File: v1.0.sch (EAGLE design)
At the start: 271 parts, among them J1 DC-044-A, J10 16p-2.54, J11 16p-2.54, J2 MICROSD-9P, J3 2p-2.54, J4 2p-2.54, J5 16p-2.54, J6 16p-2.54, J7 16p-2.54, J8 2p-2.54, J9 16p-2.54, Q1 32.768khZ@6Pf, Q2 SSM3J328R,LF, Q4 BSS138W-7-F, Q5 SSM3J328R,LF, SW1 TS-1101F, SW2 TS-1101F, SW3 TS-1101F, SW5 TS-1101F, U1 MCP23017-E/SO, U10 74HCT139D, U11 BZX84C30, U12 SP483ECN-L, U13 FT232RL-SSOP28, U14 FT232RL-SSOP28, U15 FT232RL-SSOP28, U2 MCP79412-I/SN, U3 LOPY, U4 MAX213IDBR, U5 FT232RL-SSOP28, U6 FT232RL-SSOP28, U8 BR24G32-3, Y2 12MHZ

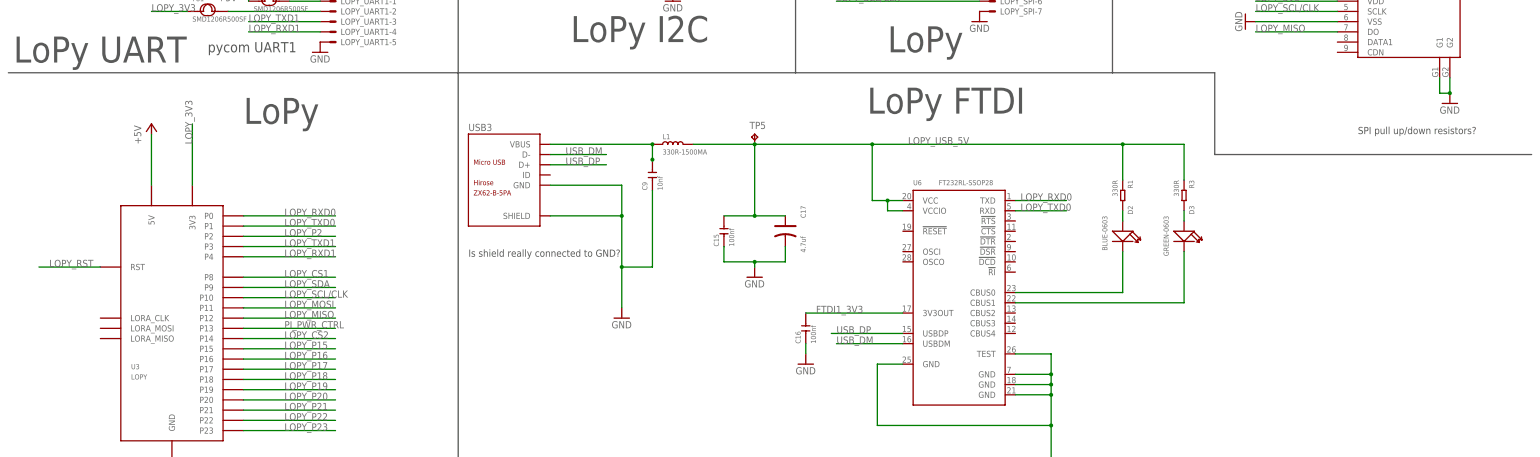
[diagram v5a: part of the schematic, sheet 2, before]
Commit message: Pi control of LoPy reset added Pi &  lopy uart0 connected
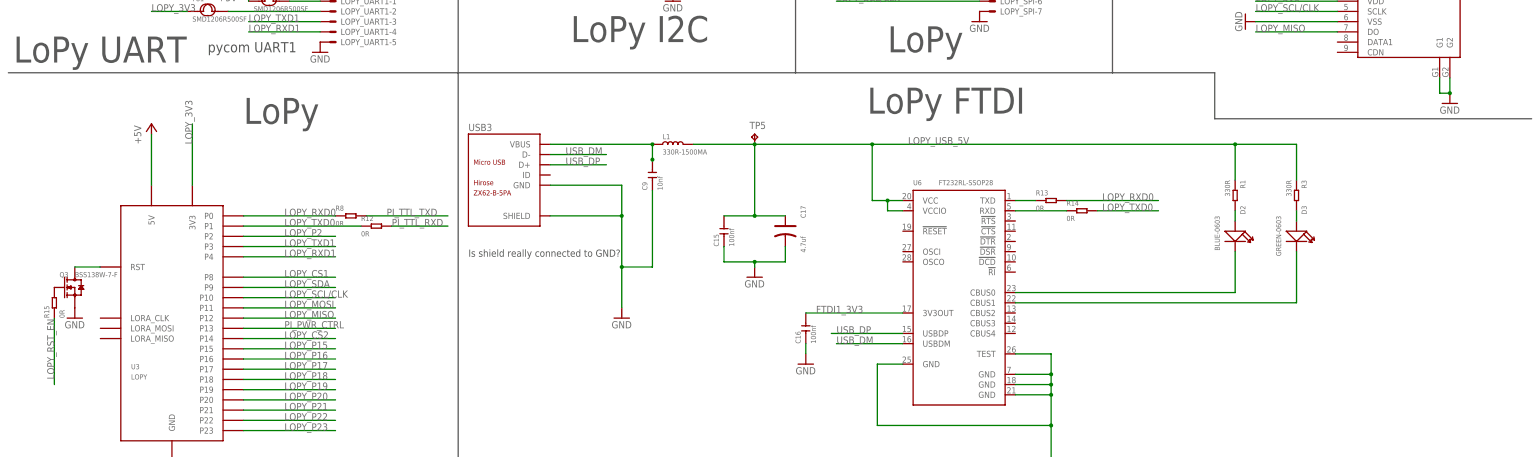
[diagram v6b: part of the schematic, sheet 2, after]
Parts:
- added Q3: BSS138W-7-F, Seeed-Transistor:SMD-MOSFET-N-CH-50V-200MA-BSS138W-7-F(SOT-23)
- added R12, R13, R14, R15, R8: 0R, Seeed-Resistor:SMD-RES-0R-5%-1/10W(0603)
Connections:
- removed net GPIO26_FREE: J10.14, J11.14, PCB1.GPIO26
- new net LOPY_RST_EN: PCB1.GPIO26, R15.1
- new net N$10: R14.1, U6.RXD
- new net N$12: Q3.G, R15.2
- new net N$8: R13.1, U6.TXD
- net GND: now also J10.14, J11.14, Q3.S
- net LOPY_RST: now also Q3.D
- net LOPY_RXD0: now also R13.2, R8.1; no longer U6.TXD
- net LOPY_TXD0: now also R12.1, R14.2; no longer U6.RXD
- net PI_TTL_RXD: now also R12.2
- net PI_TTL_TXD: now also R8.2
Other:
- note removed: "SPI pull up/down resistors?"
- moved on the sheet: D2, D3, R1, R3

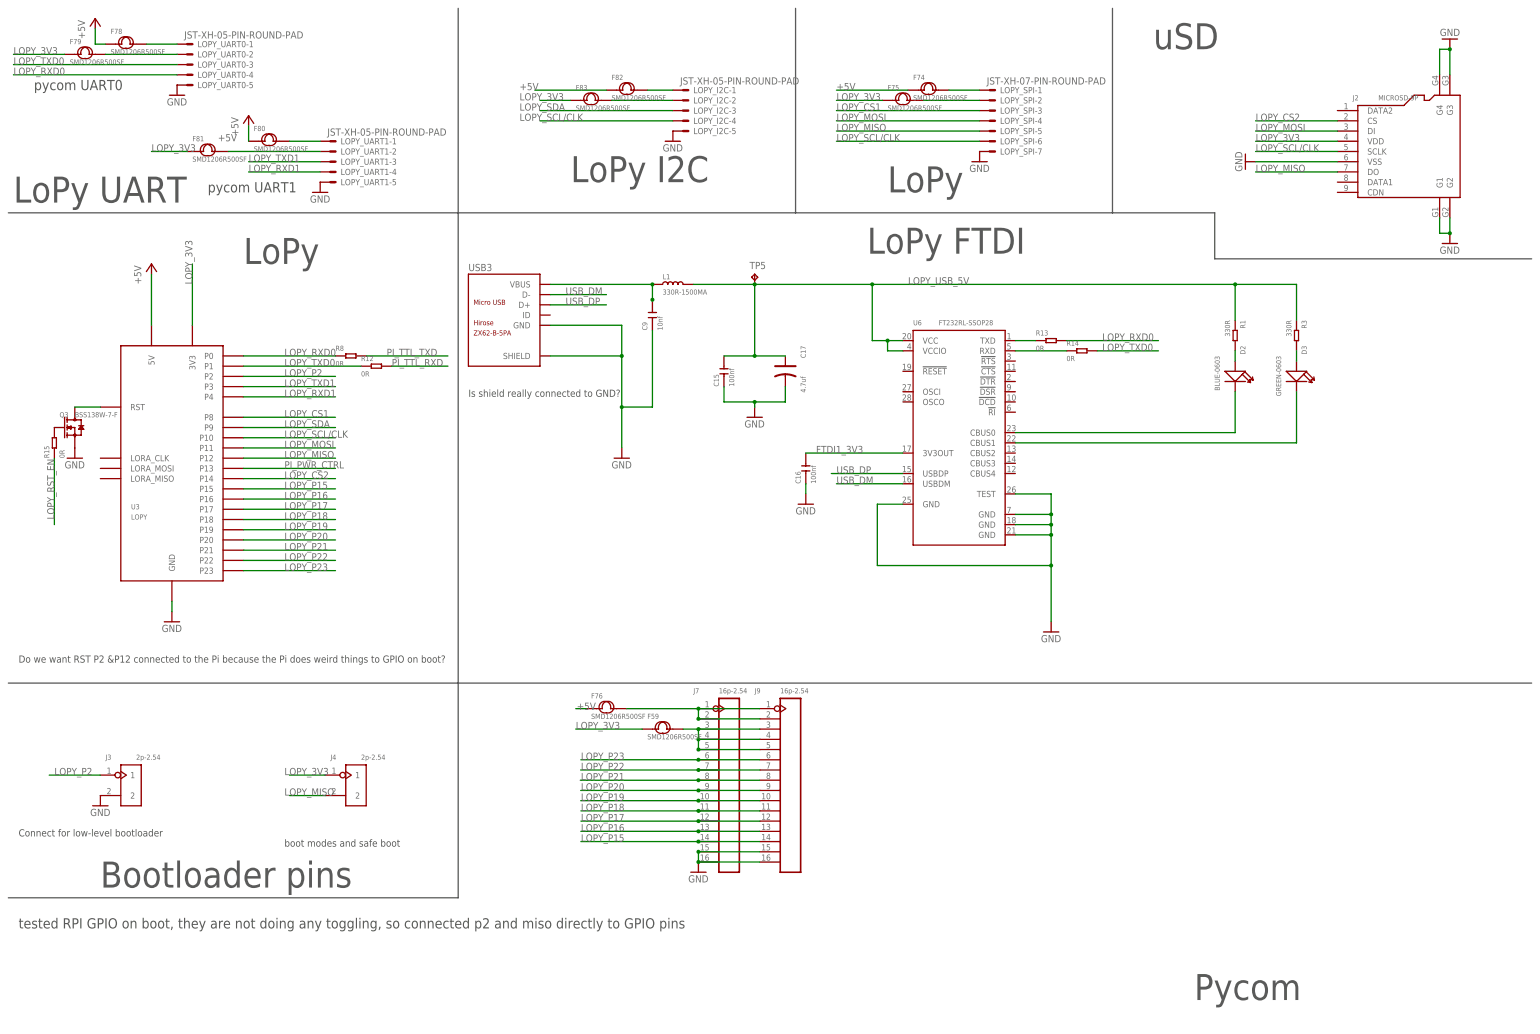
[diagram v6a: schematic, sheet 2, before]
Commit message: Switches changed for toggle as opposed to push FETs added for Pi -> lopy control lines
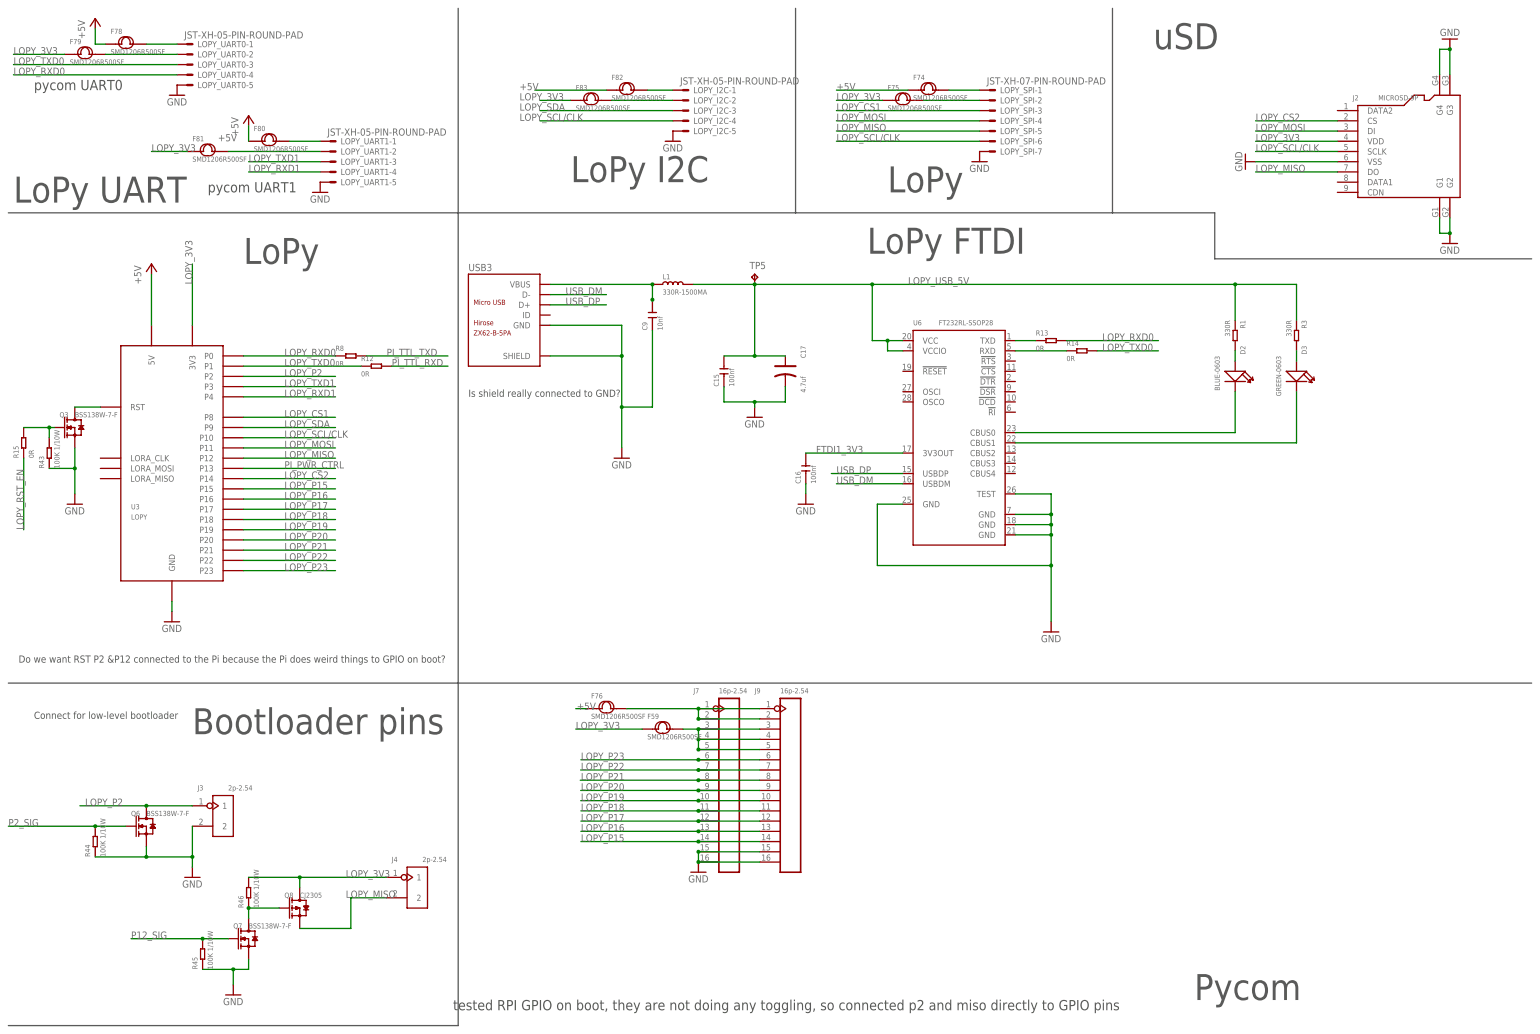
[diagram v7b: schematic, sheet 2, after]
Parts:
- removed R26: 22R, Seeed-Resistor-2016:SMD-RES-22R-5%-1/10W(0603)
- removed SW2: TS-1101F, Seeed-Switch:DIP-BUTTON(2P-6.0X3.0X4.3MM)-TS-1101F
- added Q6, Q7: BSS138W-7-F, Seeed-Transistor:SMD-MOSFET-N-CH-50V-200MA-BSS138W-7-F(SOT-23)
- added Q8: CJ2305, Seeed-Transistor:SMD-MOSFET-P-CH-8V-4.1A-CJ2305(SOT-23)
- added R43, R44, R45, R46: 100K 1/10W, Seeed-Resistor:SMD-RES-100K-5%-1/10W(0603)
- added SW4: MK-12C02 G1.5, Seeed-Switch:SMD-TOGGLE-SWITCH-ON-ON(3+4P-6.7X2.7MM)
- R25: value 100R -> 120R; device Seeed-Resistor-2016:SMD-RES-100R-5%-1/10W(0603) -> rcl:R-EU_R0603
- SW1, SW3: value TS-1101F -> MK-12C02 G1.5; device Seeed-Switch:DIP-BUTTON(2P-6.0X3.0X4.3MM)-TS-1101F -> Seeed-Switch:SMD-TOGGLE-SWITCH-ON-ON(3+4P-6.7X2.7MM)
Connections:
- net LOPY_MISO_AFTER renamed GPIO16
- net LOPY_P2_AFTER renamed GPIO5
- removed net N$47: R25.2, R26.1
- new net N$13: Q7.D, Q8.G, R46.1
- new net P12_SIG: Q7.G, R17.1, R45.2
- new net P2_SIG: Q6.G, R41.1, R44.2
- net GND: now also Q6.S, Q7.S, R43.1, R44.1, R45.1, SW1.SS1, SW1.SS2, SW1.SS3, SW1.SS4, SW3.SS1, SW3.SS2, SW3.SS3, SW3.SS4, SW4.COM, SW4.SS1, SW4.SS2, SW4.SS3, SW4.SS4; no longer SW1.2
- net LED_GND: now also SW4.B; no longer SW1.1
- net LOPY_3V3: now also Q8.D, R46.2, SW3.B; no longer SW2.1
- net LOPY_MISO: now also Q8.S; no longer R17.1
- net LOPY_P2: now also Q6.D; no longer R41.1
- net N$12: now also R43.2
- net N$9: now also SW1.B; no longer SW3.1
- net PI_PWR_CTRL: now also SW3.COM; no longer SW2.2
- net RS485_A: now also SW1.COM; no longer SW3.2
- net RS485_B: now also R25.2; no longer R26.2
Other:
- note removed: "Seed does not have 120R resistors, so put a 100R and 22R resistors in series."
- note removed: "boot modes and safe boot"
- moved on the sheet: J3, J4, R15, TP9

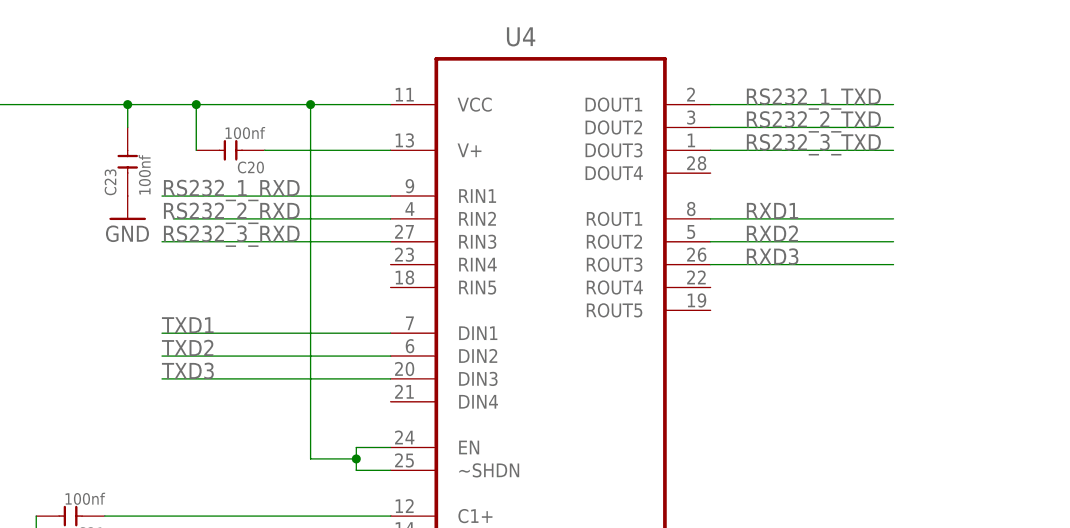
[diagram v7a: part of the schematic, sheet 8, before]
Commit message: Now has 2 TTL serial ports
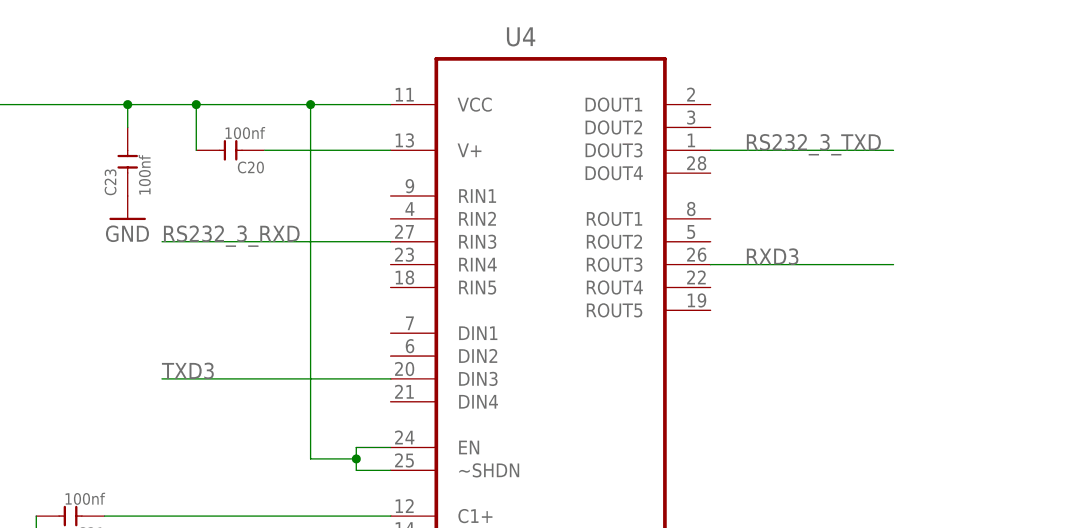
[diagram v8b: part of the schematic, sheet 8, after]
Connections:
- removed net RS232_1_RXD: I_UART_HUB_1-4.S, U4.RIN1
- removed net RS232_1_TXD: I_UART_HUB_1-3.S, U4.DOUT1
- removed net RS232_2_RXD: PI_UART_HUB_2-4.S, U4.RIN2
- removed net RS232_2_TXD: PI_UART_HUB_2-3.S, U4.DOUT2
- net RXD1: now also I_UART_HUB_1-4.S; no longer U4.ROUT1
- net RXD2: now also PI_UART_HUB_2-4.S; no longer U4.ROUT2
- net TXD1: now also I_UART_HUB_1-3.S; no longer U4.DIN1
- net TXD2: now also PI_UART_HUB_2-3.S; no longer U4.DIN2
